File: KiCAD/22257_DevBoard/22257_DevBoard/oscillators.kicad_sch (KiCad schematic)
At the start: 6 parts

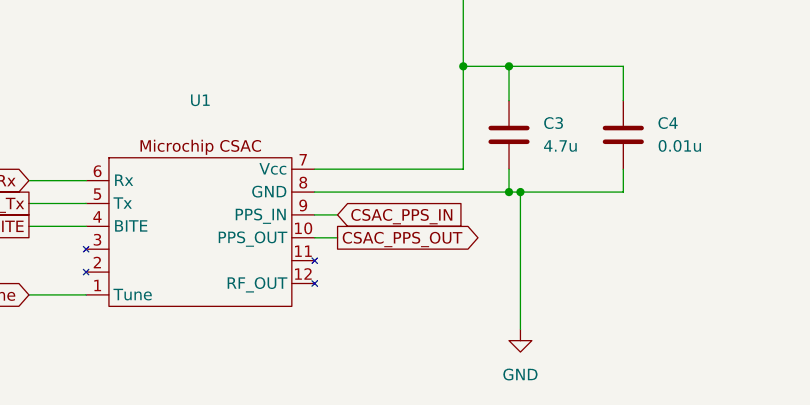
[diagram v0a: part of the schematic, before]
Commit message: Schematic Progress. Added connections to the MicroZed and added a 3v3 rail regulator
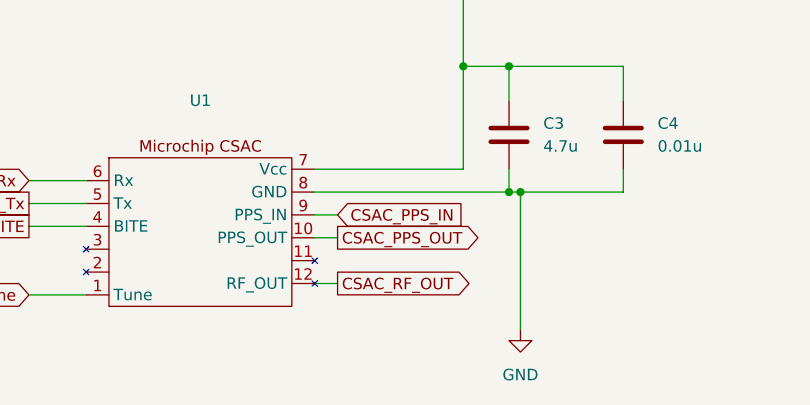
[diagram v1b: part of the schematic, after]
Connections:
- net CSAC_RF_OUT: now reaches U1.12 (RF_OUT)
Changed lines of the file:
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@@
+	(wire
+		(pts
+			(xy 100.33 71.12) (xy 102.87 71.12)
+		)
+		(stroke
+			(width 0)
+			(type default)
+		)
+	)
 	(wire
 		(pts
@@
 			(effects
 				(font
+					(size 1.27 1.27)
+				)
+				(justify left)
+				(hide yes)
+			)
+		)
+	)
+	(global_label "CSAC_RF_OUT"
+		(shape output)
+		(at 102.87 71.12 0)
+		(fields_autoplaced yes)
+		(effects
+			(font
+				(size 1.27 1.27)
+			)
+			(justify left)
+		)
+		(property "Intersheetrefs" "${INTERSHEET_REFS}"
+			(at 118.6157 71.12 0)
+			(effects
+				(font

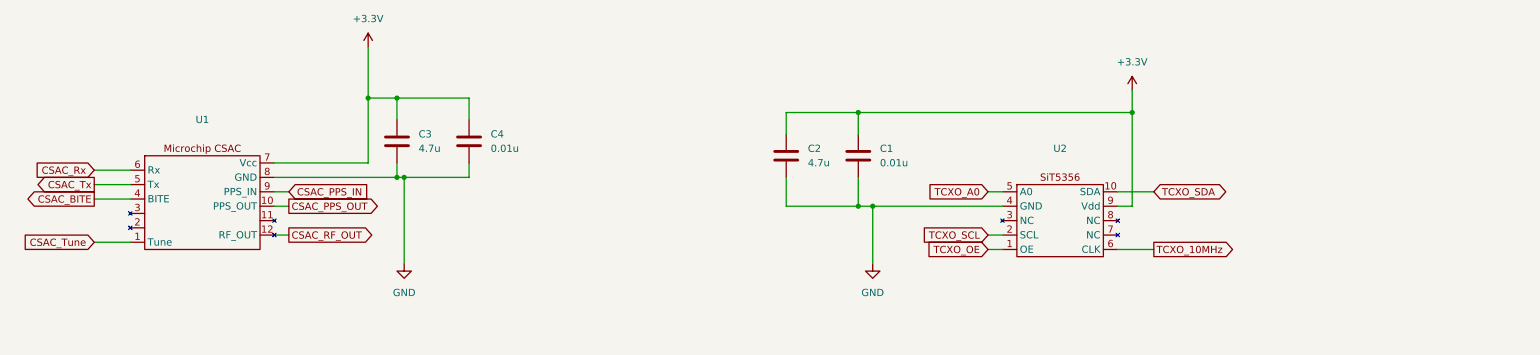
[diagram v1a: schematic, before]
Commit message: More Schematic Updates
Added power monitors and connectors, along with finishing the power circuitry.
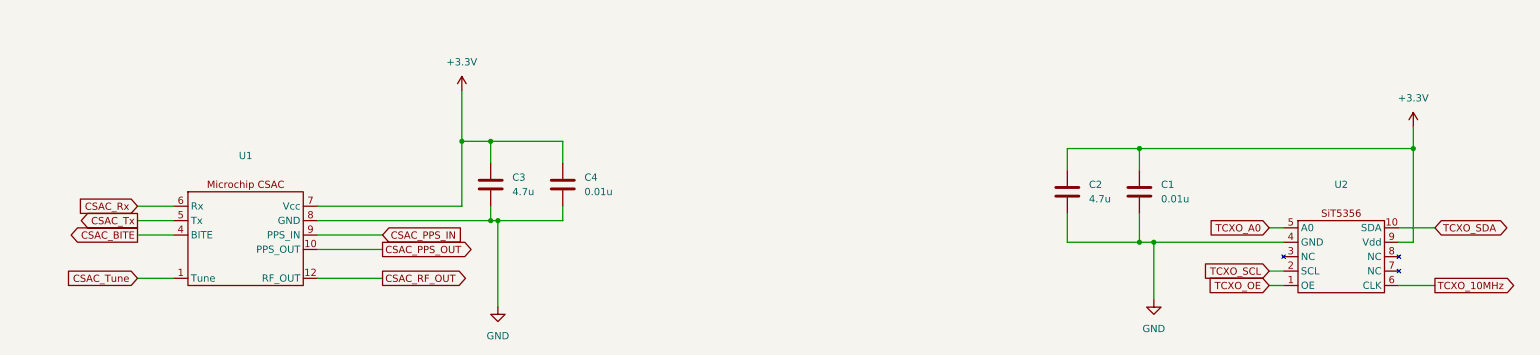
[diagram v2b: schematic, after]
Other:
- moved on the sheet: C1, C2, C3, C4, U2

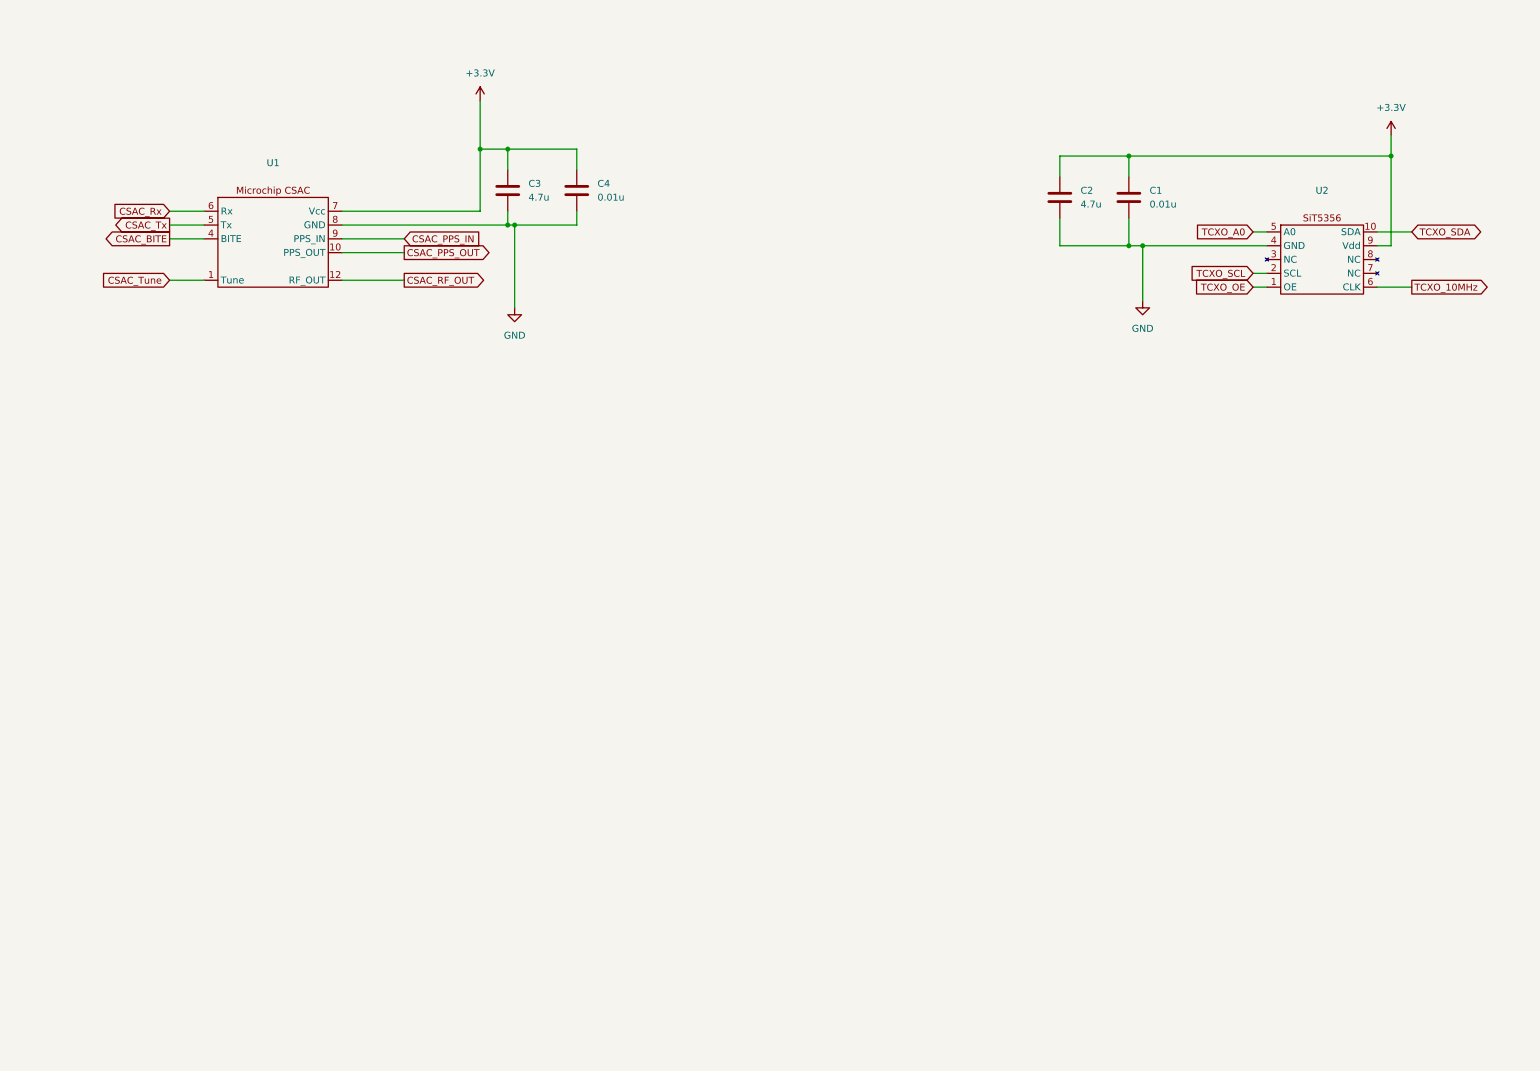
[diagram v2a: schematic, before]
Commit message: Schematic should be finished, onto layout
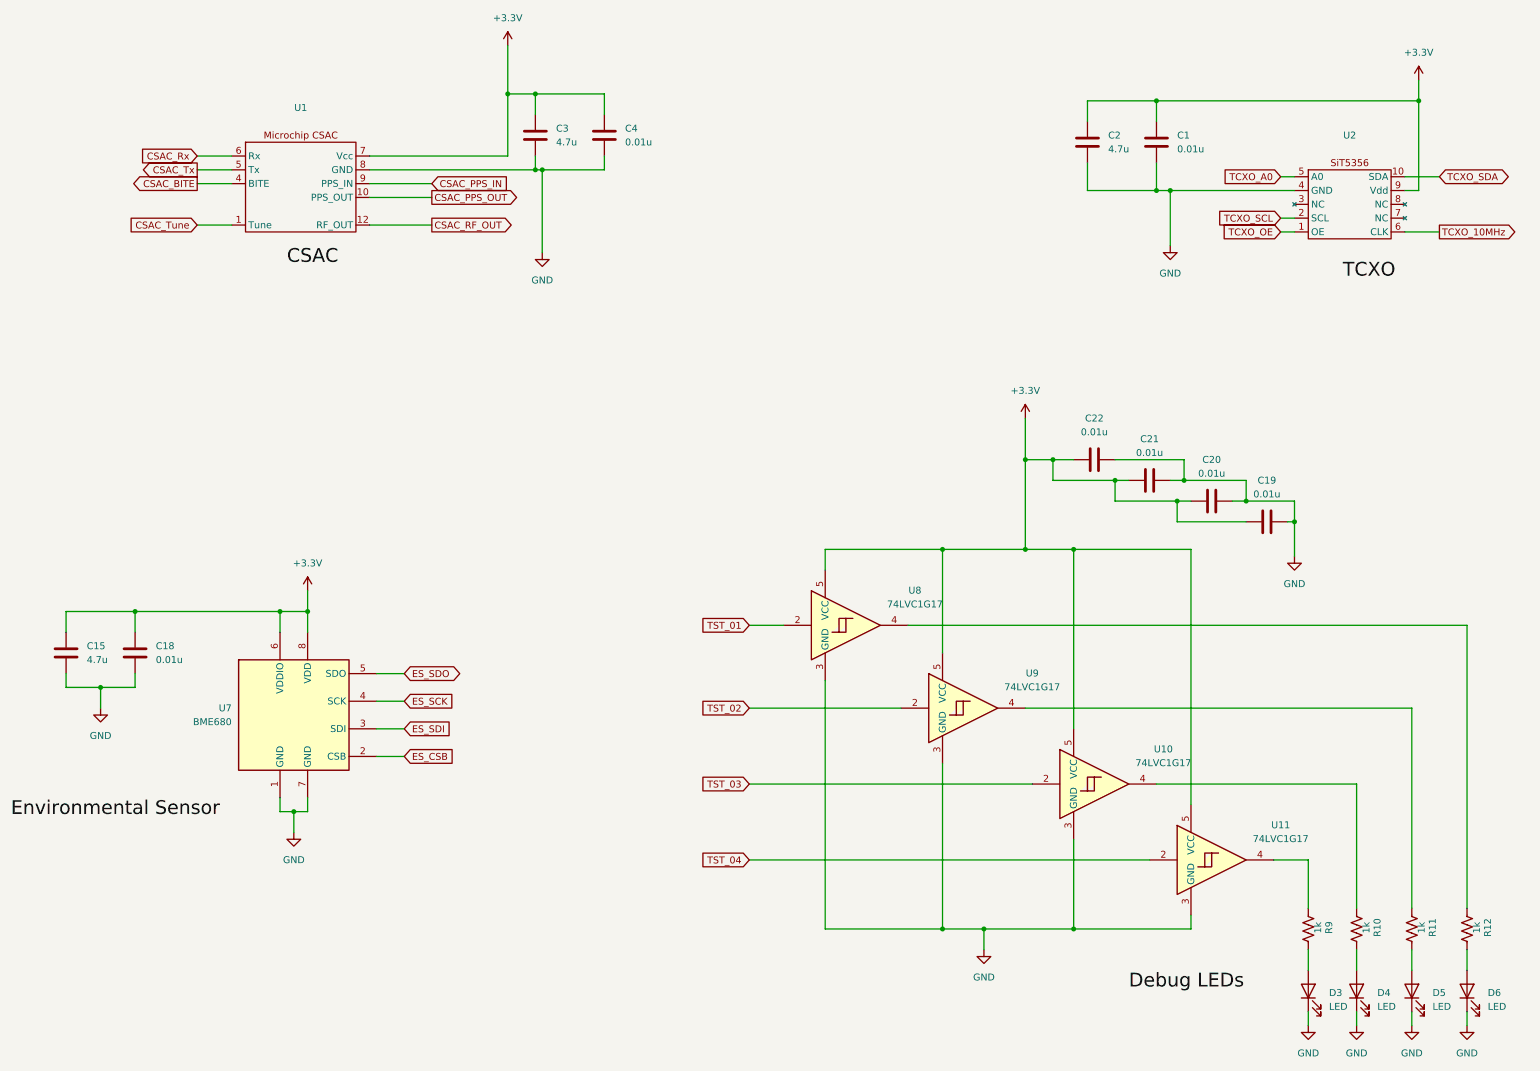
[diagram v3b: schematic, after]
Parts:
- added C15: 4.7u, symbol Device:C
- added C18, C19, C20, C21, C22: 0.01u, symbol Device:C
- added D3, D4, D5, D6: LED, symbol Device:LED
- added R10, R11, R12, R9: 1k, symbol Device:R_US
- added U10, U11, U8, U9: 74LVC1G17, symbol 74xGxx:74LVC1G17
- added U7: BME680, Package_LGA:Bosch_LGA-8_3x3mm_P0.8mm_ClockwisePinNumbering, symbol Sensor:BME680
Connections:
- net +3.3V: now also C15.1, C18.1, C19.1, C20.1, C21.1, C22.1, U10.5 (VCC), U11.5 (VCC), U7.6 (VDDIO), U7.8 (VDD), U8.5 (VCC), U9.5 (VCC)
- net GND: now also C15.2, C18.2, C19.2, C20.2, C21.2, C22.2, D3.1 (K), D4.1 (K), D5.1 (K), D6.1 (K), U10.3 (GND), U11.3 (GND), U7.1 (GND), U7.7 (GND), U8.3 (GND), U9.3 (GND)
- new net: D3.2 (A), R9.1
- new net: R9.2, U11.4
- new net: D5.2 (A), R11.1
- new net: R11.2, U9.4
- new net: R10.2, U10.4
- new net: D6.2 (A), R12.1
- new net: R12.2, U8.4
- new net: D4.2 (A), R10.1
- new net ES_CSB: U7.2 (CSB)
- new net ES_SCK: U7.4 (SCK)
- new net ES_SDI: U7.3 (SDI)
- new net ES_SDO: U7.5 (SDO)
- new net TST_01: U8.2
- new net TST_02: U9.2
- new net TST_03: U10.2
- new net TST_04: U11.2
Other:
- moved on the sheet: C1, C2, C3, C4, U1, U2
